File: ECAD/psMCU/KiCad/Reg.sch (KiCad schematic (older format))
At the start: 16 parts, among them U258 SN74LVC1G04DCK, U259 CD74HC173PW, U260 CD74HC173PW, U261 SN74LVC1G126DCK, U262 SN74LVC1G04DCK, U263 SN74HC245PW

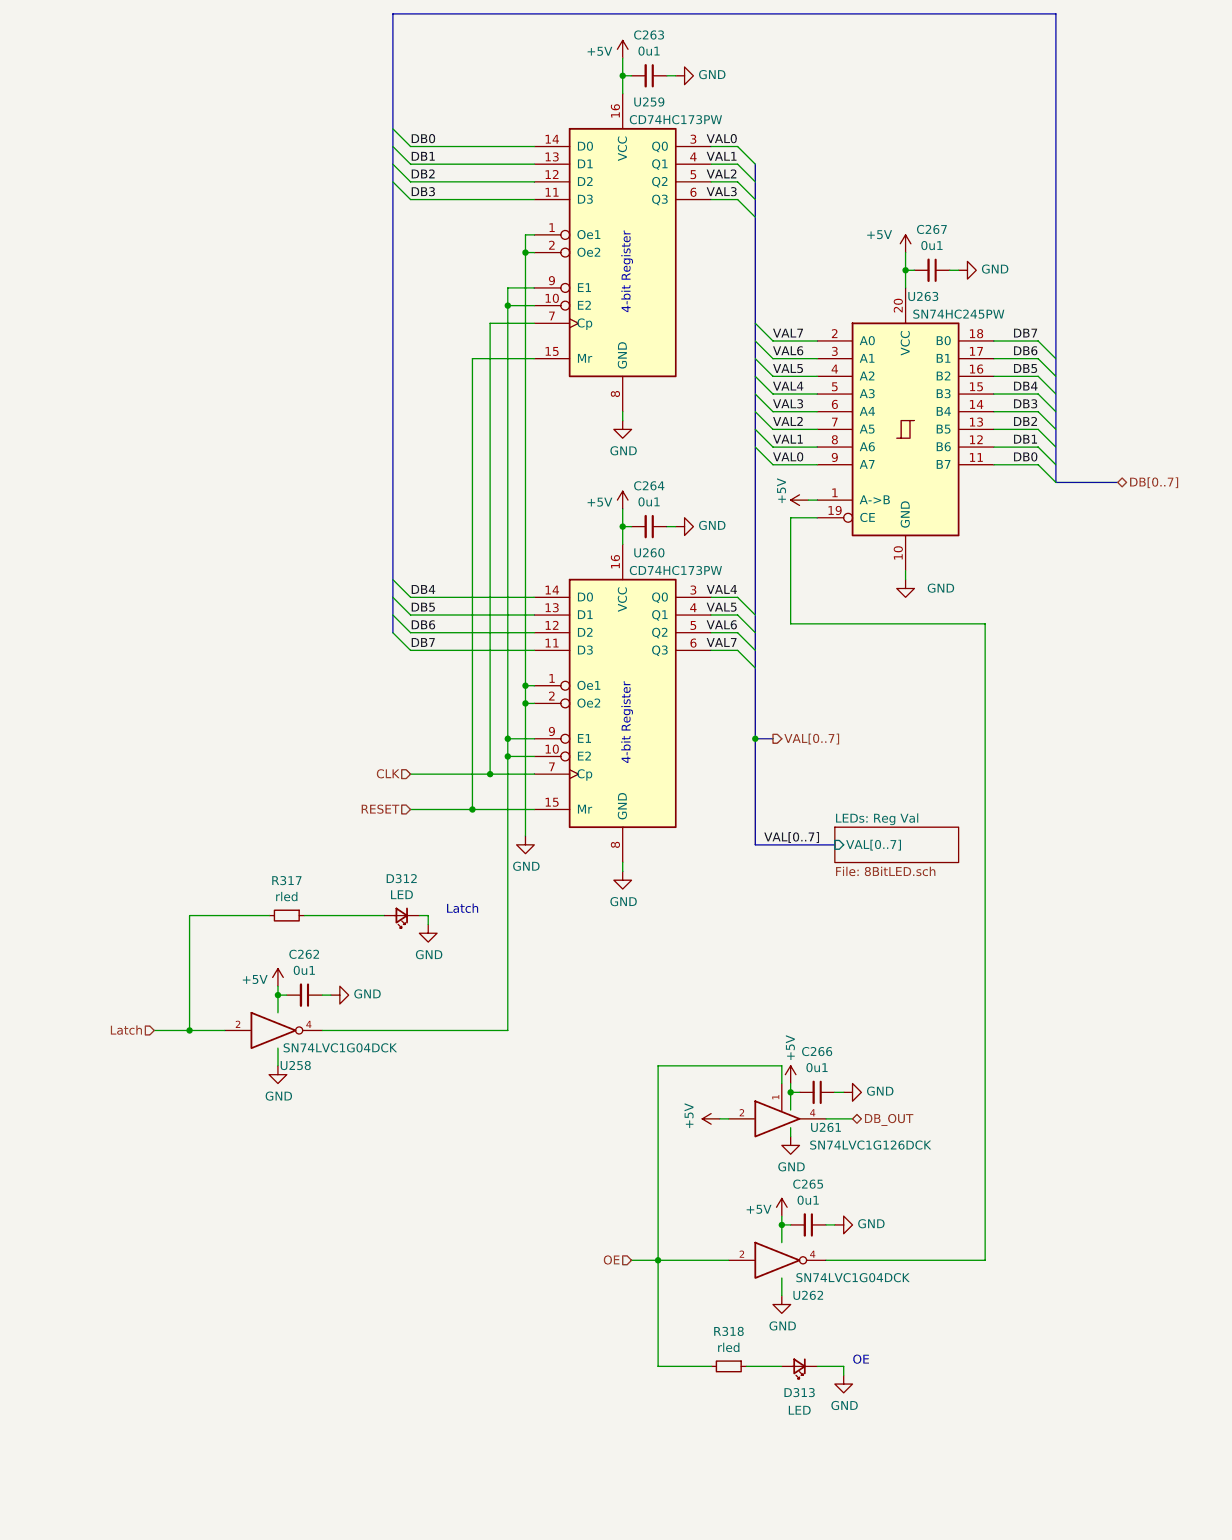
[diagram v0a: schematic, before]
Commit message: Sch: Removed Regulator, Added extra spread bulk C
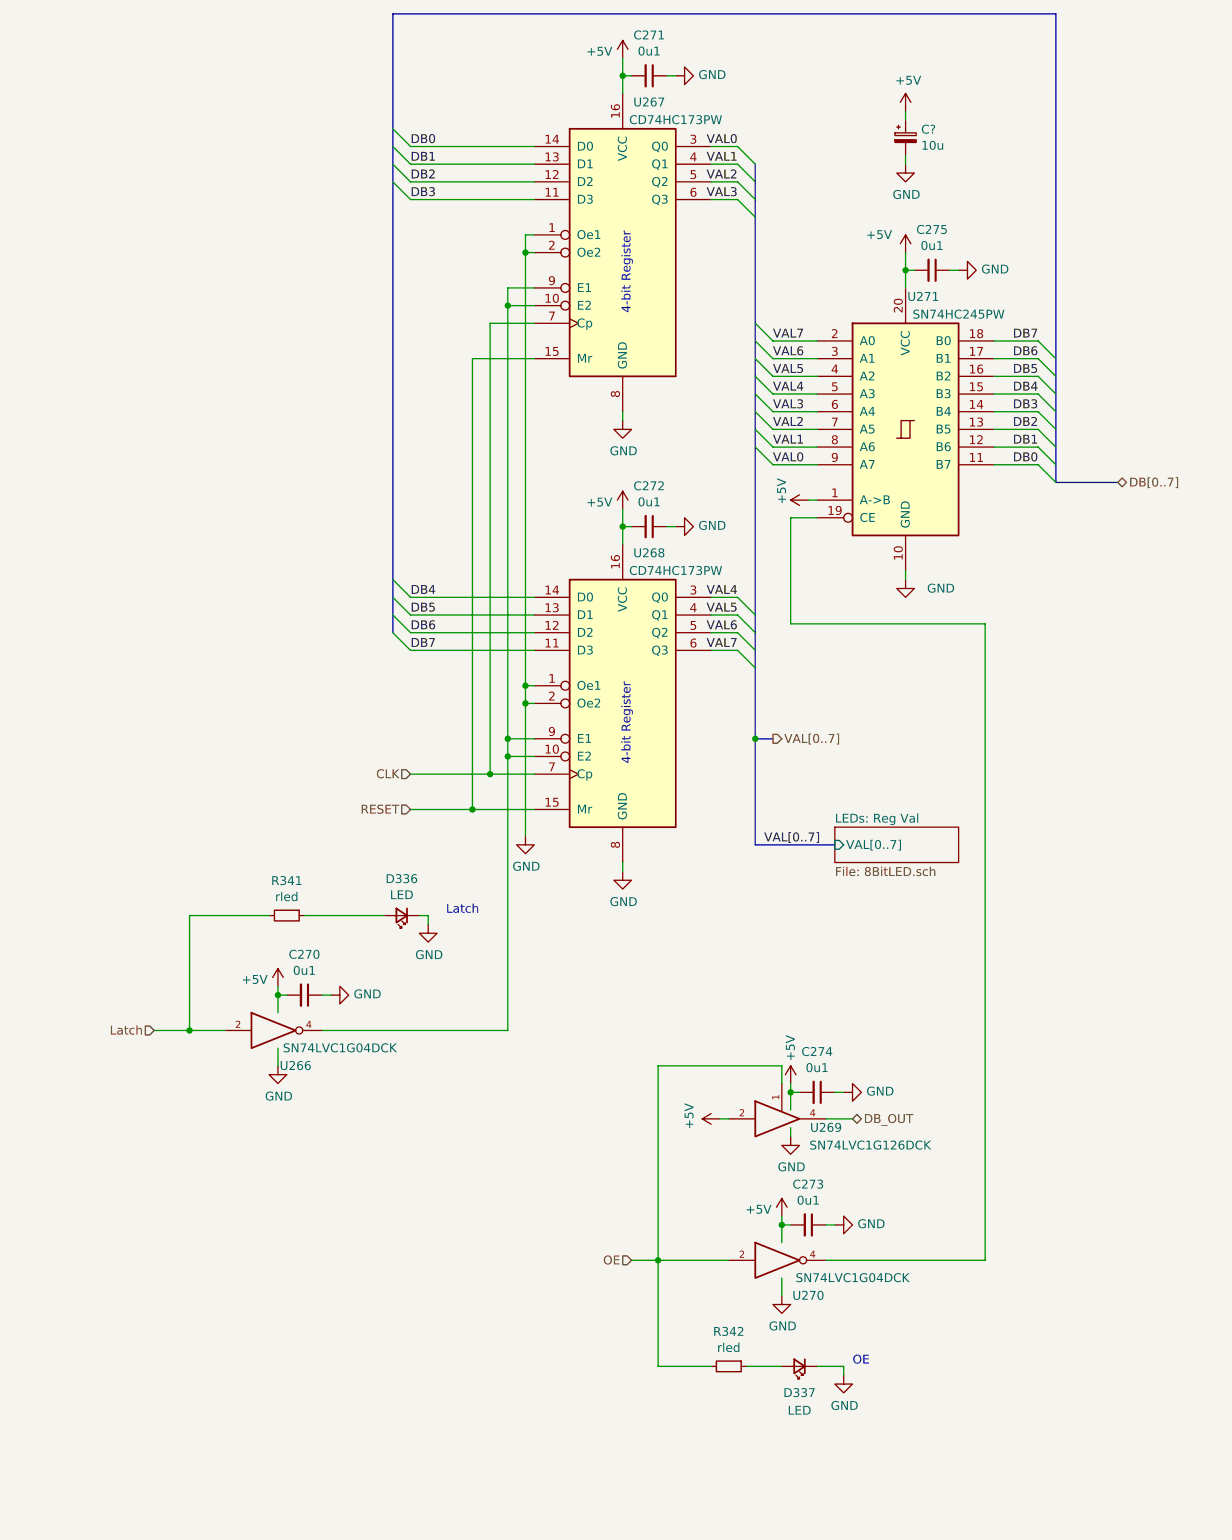
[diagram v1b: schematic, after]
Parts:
- added C?: 10u, symbol Device:CP_Small
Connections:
- net +5V: now also C?.1
- net GND: now also C?.2
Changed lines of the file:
@@
 $Descr A4 8268 11693 portrait
 encoding utf-8
-Sheet 58 97
+Sheet 60 97
 Title "psMCU"
 Date "2022-02-13"
@@
 AR Path="/61C3CF7F/5F0B921F" Ref="U262"  Part="1"
 AR Path="/61C3CF88/5F0B921F" Ref="U270"  Part="1"
-F 0 "U262" H 4950 7900 50  0000 C CNN
+F 0 "U270" H 4950 7900 50  0000 C CNN
 F 1 "SN74LVC1G04DCK" H 5200 8000 50  0000 C CNN
 F 2 "Package_TO_SOT_SMD:SOT-353_SC-70-5" H 4800 8100 50  0001 C CNN
@@
 AR Path="/61C3CF7F/5F0B922C" Ref="C265"  Part="1"
 AR Path="/61C3CF88/5F0B922C" Ref="C273"  Part="1"
-F 0 "C265" V 4721 7900 50  0000 C CNN
+F 0 "C273" V 4721 7900 50  0000 C CNN
 F 1 "0u1" V 4812 7900 50  0000 C CNN
 F 2 "NoRef_Footprints:C_0603_1608Metric_NoRef" H 4950 7900 50  0001 C CNN
@@
 AR Path="/61C3CF7F/5EF8C8C3" Ref="C262"  Part="1"
 AR Path="/61C3CF88/5EF8C8C3" Ref="C270"  Part="1"
-F 0 "C262" V 1871 6600 50  0000 C CNN
+F 0 "C270" V 1871 6600 50  0000 C CNN
 F 1 "0u1" V 1962 6600 50  0000 C CNN
 F 2 "NoRef_Footprints:C_0603_1608Metric_NoRef" H 2100 6600 50  0001 C CNN
@@
 AR Path="/61C3CF7F/5EF829AC" Ref="U258"  Part="1"
 AR Path="/61C3CF88/5EF829AC" Ref="U266"  Part="1"
-F 0 "U258" H 2050 6600 50  0000 C CNN
+F 0 "U266" H 2050 6600 50  0000 C CNN
 F 1 "SN74LVC1G04DCK" H 2300 6700 50  0000 C CNN
 F 2 "Package_TO_SOT_SMD:SOT-353_SC-70-5" H 1950 6800 50  0001 C CNN
@@
 AR Path="/61C3CF7F/5ED710F5" Ref="C267"  Part="1"
 AR Path="/61C3CF88/5ED710F5" Ref="C275"  Part="1"
-F 0 "C267" V 5421 2500 50  0000 C CNN
+F 0 "C275" V 5421 2500 50  0000 C CNN
 F 1 "0u1" V 5512 2500 50  0000 C CNN
 F 2 "NoRef_Footprints:C_0603_1608Metric_NoRef" H 5650 2500 50  0001 C CNN
@@
 AR Path="/61C3CF7F/5ED4E5FA" Ref="U263"  Part="1"
 AR Path="/61C3CF88/5ED4E5FA" Ref="U271"  Part="1"
-F 0 "U263" H 5600 4150 50  0000 C CNN
+F 0 "U271" H 5600 4150 50  0000 C CNN
 F 1 "SN74HC245PW" H 5800 4050 50  0000 C CNN
 F 2 "Package_SO:TSSOP-20_4.4x6.5mm_P0.65mm" H 5500 3400 50  0001 C CNN
@@
 AR Path="/61C3CF7F/5ED33B48" Ref="C264"  Part="1"
 AR Path="/61C3CF88/5ED33B48" Ref="C272"  Part="1"
-F 0 "C264" V 3821 3950 50  0000 C CNN
+F 0 "C272" V 3821 3950 50  0000 C CNN
 F 1 "0u1" V 3912 3950 50  0000 C CNN
 F 2 "NoRef_Footprints:C_0603_1608Metric_NoRef" H 4050 3950 50  0001 C CNN
@@
 AR Path="/61C3CF7F/5ED33B3B" Ref="U260"  Part="1"
 AR Path="/61C3CF88/5ED33B3B" Ref="U268"  Part="1"
-F 0 "U260" H 4050 5800 50  0000 C CNN
+F 0 "U268" H 4050 5800 50  0000 C CNN
 F 1 "CD74HC173PW" H 4200 5700 50  0000 C CNN
 F 2 "Package_SO:TSSOP-16_4.4x5mm_P0.65mm" H 3900 4950 50  0001 C CNN
@@
 AR Path="/61C3CF7F/5ED2F1C3" Ref="C263"  Part="1"
 AR Path="/61C3CF88/5ED2F1C3" Ref="C271"  Part="1"
-F 0 "C263" V 3821 1400 50  0000 C CNN
+F 0 "C271" V 3821 1400 50  0000 C CNN
 F 1 "0u1" V 3912 1400 50  0000 C CNN
 F 2 "NoRef_Footprints:C_0603_1608Metric_NoRef" H 4050 1400 50  0001 C CNN
@@
 AR Path="/61C3CF7F/5ED2BCE4" Ref="U259"  Part="1"
 AR Path="/61C3CF88/5ED2BCE4" Ref="U267"  Part="1"
-F 0 "U259" H 4050 3250 50  0000 C CNN
+F 0 "U267" H 4050 3250 50  0000 C CNN
 F 1 "CD74HC173PW" H 4200 3150 50  0000 C CNN
 F 2 "Package_SO:TSSOP-16_4.4x5mm_P0.65mm" H 3900 2400 50  0001 C CNN
@@
 AR Path="/61C3CF7F/5F369738" Ref="C266"  Part="1"
 AR Path="/61C3CF88/5F369738" Ref="C274"  Part="1"
-F 0 "C266" V 4771 7150 50  0000 C CNN
+F 0 "C274" V 4771 7150 50  0000 C CNN
 F 1 "0u1" V 4862 7150 50  0000 C CNN
 F 2 "NoRef_Footprints:C_0603_1608Metric_NoRef" H 5000 7150 50  0001 C CNN
@@
 AR Path="/61C3CF7F/62B8F34C" Ref="D313"  Part="1"
 AR Path="/61C3CF88/62B8F34C" Ref="D337"  Part="1"
-F 0 "D313" H 4900 8850 50  0000 C CNN
+F 0 "D337" H 4900 8850 50  0000 C CNN
 F 1 "LED" H 4900 8950 50  0000 C CNN
 F 2 "NoRef_Footprints:D_0603_1608Metric_NoRef" V 4900 8700 50  0001 C CNN
@@
 AR Path="/61C3CF7F/62B8F35A" Ref="R318"  Part="1"
 AR Path="/61C3CF88/62B8F35A" Ref="R342"  Part="1"
-F 0 "R318" V 4304 8700 50  0000 C CNN
+F 0 "R342" V 4304 8700 50  0000 C CNN
 F 1 "rled" V 4395 8700 50  0000 C CNN
 F 2 "NoRef_Footprints:R_0603_1608Metric_NoRef" H 4500 8700 50  0001 C CNN
@@
 AR Path="/61C3CF7F/62B948BD" Ref="D312"  Part="1"
 AR Path="/61C3CF88/62B948BD" Ref="D336"  Part="1"
-F 0 "D312" H 2650 5943 50  0000 C CNN
+F 0 "D336" H 2650 5943 50  0000 C CNN
 F 1 "LED" H 2650 6034 50  0000 C CNN
 F 2 "NoRef_Footprints:D_0603_1608Metric_NoRef" V 2650 6150 50  0001 C CNN
@@
 AR Path="/61C3CF7F/62B948CB" Ref="R317"  Part="1"
 AR Path="/61C3CF88/62B948CB" Ref="R341"  Part="1"
-F 0 "R317" V 1804 6150 50  0000 C CNN
+F 0 "R341" V 1804 6150 50  0000 C CNN
 F 1 "rled" V 1895 6150 50  0000 C CNN
 F 2 "NoRef_Footprints:R_0603_1608Metric_NoRef" H 2000 6150 50  0001 C CNN
@@
 AR Path="/61C3CF7F/5F369721" Ref="U261"  Part="1"
 AR Path="/61C3CF88/5F369721" Ref="U269"  Part="1"
-F 0 "U261" H 5050 7250 50  0000 C CNN
+F 0 "U269" H 5050 7250 50  0000 C CNN
 F 1 "SN74LVC1G126DCK" H 5300 7150 50  0000 C CNN
 F 2 "Package_TO_SOT_SMD:SOT-353_SC-70-5" H 4800 7300 50  0001 C CNN
@@
 Text Notes 5200 8700 0    50   ~ 0
 OE
+$Comp
+L Device:CP_Small C?
+U 1 1 6244A237
+P 5500 1750
+AR Path="/62043340/6244A237" Ref="C?"  Part="1"
+AR Path="/61C3CF88/6244A237" Ref="C?"  Part="1"
+F 0 "C?" H 5588 1796 50  0000 L CNN
+F 1 "10u" H 5588 1705 50  0000 L CNN
+F 2 "" H 5500 1750 50  0001 C CNN
+F 3 "~" H 5500 1750 50  0001 C CNN
+	1    5500 1750
+	1    0    0    -1
+$EndComp
+$Comp
+L power:GND #PWR?
+U 1 1 6244A23D
+P 5500 1900
+AR Path="/6244A23D" Ref="#PWR?"  Part="1"
+AR Path="/62043340/6244A23D" Ref="#PWR?"  Part="1"
+AR Path="/61C3CF88/6244A23D" Ref="#PWR?"  Part="1"
+F 0 "#PWR?" H 5500 1650 50  0001 C CNN
+F 1 "GND" H 5505 1727 50  0000 C CNN
+F 2 "" H 5500 1900 50  0001 C CNN
+F 3 "" H 5500 1900 50  0001 C CNN
+	1    5500 1900
+	1    0    0    -1
+$EndComp
+Wire Wire Line
+	5500 1900 5500 1850
+Wire Wire Line
+	5500 1600 5500 1650
+$Comp
+L power:+5V #PWR?
+U 1 1 6244A245
+P 5500 1600
+AR Path="/6244A245" Ref="#PWR?"  Part="1"
+AR Path="/62043340/6244A245" Ref="#PWR?"  Part="1"
+AR Path="/61C3CF88/6244A245" Ref="#PWR?"  Part="1"
+F 0 "#PWR?" H 5500 1450 50  0001 C CNN
+F 1 "+5V" H 5515 1773 50  0000 C CNN
+F 2 "" H 5500 1600 50  0001 C CNN
+F 3 "" H 5500 1600 50  0001 C CNN
+	1    5500 1600
+	1    0    0    -1
+$EndComp
 Wire Bus Line
 	2600 1050 2600 4550

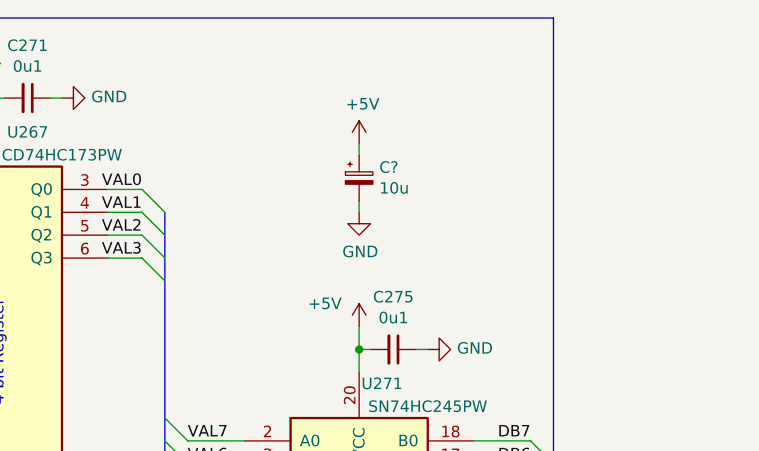
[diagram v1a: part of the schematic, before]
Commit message: Sch: Reworked Peripheral Interface (Buffers)
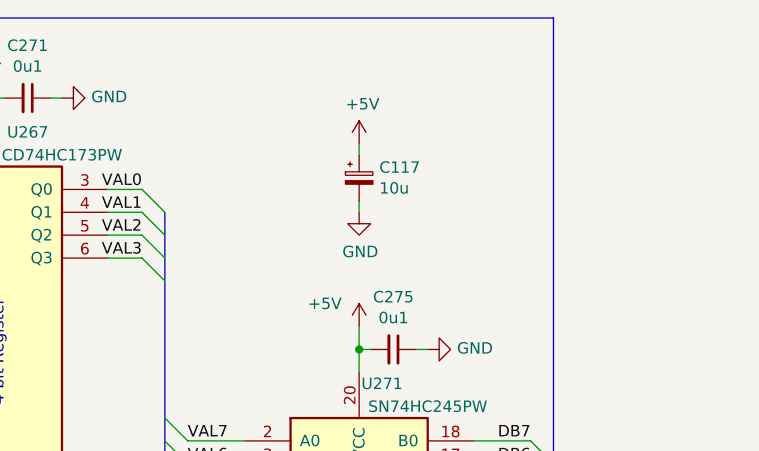
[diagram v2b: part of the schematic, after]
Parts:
- gave numbers to parts that had none: 1
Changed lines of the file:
@@
 $Descr A4 8268 11693 portrait
 encoding utf-8
-Sheet 60 97
+Sheet 60 96
 Title "psMCU"
 Date "2022-02-13"
@@
 P 5500 1750
 AR Path="/62043340/6244A237" Ref="C?"  Part="1"
-AR Path="/61C3CF88/6244A237" Ref="C?"  Part="1"
-F 0 "C?" H 5588 1796 50  0000 L CNN
+AR Path="/61C3CF88/6244A237" Ref="C117"  Part="1"
+AR Path="/61C3CF7F/6244A237" Ref="C116"  Part="1"
+F 0 "C117" H 5588 1796 50  0000 L CNN
 F 1 "10u" H 5588 1705 50  0000 L CNN
 F 2 "" H 5500 1750 50  0001 C CNN
@@
 AR Path="/6244A23D" Ref="#PWR?"  Part="1"
 AR Path="/62043340/6244A23D" Ref="#PWR?"  Part="1"
-AR Path="/61C3CF88/6244A23D" Ref="#PWR?"  Part="1"
-F 0 "#PWR?" H 5500 1650 50  0001 C CNN
+AR Path="/61C3CF88/6244A23D" Ref="#PWR01446"  Part="1"
+AR Path="/61C3CF7F/6244A23D" Ref="#PWR01444"  Part="1"
+F 0 "#PWR01446" H 5500 1650 50  0001 C CNN
 F 1 "GND" H 5505 1727 50  0000 C CNN
 F 2 "" H 5500 1900 50  0001 C CNN
@@
 AR Path="/6244A245" Ref="#PWR?"  Part="1"
 AR Path="/62043340/6244A245" Ref="#PWR?"  Part="1"
-AR Path="/61C3CF88/6244A245" Ref="#PWR?"  Part="1"
-F 0 "#PWR?" H 5500 1450 50  0001 C CNN
+AR Path="/61C3CF88/6244A245" Ref="#PWR01447"  Part="1"
+AR Path="/61C3CF7F/6244A245" Ref="#PWR01445"  Part="1"
+F 0 "#PWR01447" H 5500 1450 50  0001 C CNN
 F 1 "+5V" H 5515 1773 50  0000 C CNN
 F 2 "" H 5500 1600 50  0001 C CNN
